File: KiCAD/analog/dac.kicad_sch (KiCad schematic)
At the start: 18 parts, among them Q11 2N3904, Q12 2N3904, U4 MCP4922-EP, U9 74HCT125

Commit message: revD analog: DGFET op-amp offset-mute topology + doc updates
Retire the Q11/Q12 PNP KeyUp mute path on the DGFET keyer G2 (sim showed
only ~2.6:1 on/off ratio with G1 biased above V_TO). Replace with an
LM7171 (U10) non-inverting op-amp wired as DC offset:
  V_G2 = V_DAC * (1 + R20/R23) - V_ref * (R20/R23)
with V_ref ~5.05V (1N4733A Zener D2, R24 1K bias, R25 1K / R32 100K
summing divider) and R20=6.2K / R23=10K (G=0.62). DAC=0 drives G2 to
-3.1V (fully cuts off the 40673, sim-verified 12pA leakage, ~10^9 on/off
ratio); DAC=5V drives G2 to +5V (matches prior keyed operating point).
KEY_UP net eliminated -- mute is intrinsic to the signal path, firmware
controls RF enable/disable solely via what it writes to the MCP4921
envelope channel.

Includes new test.kicad_sch sheet carrying the U10/R20-R32 subcircuit.

Doc updates: CLAUDE.md DGFET section rewritten; handoff doc gets a new
"DGFET keyer mute topology" section explaining retirement reason and
new transfer function; Master_Description Sec 2 and SPI-bus section
updated; revD_interconnect G2 amplitude-control block updated;
control_board_functional_blocks.md gets a prominent retirement banner
pointing at the current scheme.

Co-Authored-By: Claude Opus 4.7 <noreply@anthropic.com>
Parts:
- removed C51: 10uF, Capacitor_THT:CP_Radial_D5.0mm_P2.00mm, symbol Device:C_Polarized_US
- removed C92: 100nF, Capacitor_THT:C_Disc_D5.0mm_W2.5mm_P5.00mm, symbol Device:C_Small
- removed Q11, Q12: 2N3904, Package_TO_SOT_THT:TO-92_Inline_Wide, symbol Transistor_BJT:2N3904
- removed R48, R50, R51: 10K, Resistor_THT:R_Axial_DIN0207_L6.3mm_D2.5mm_P10.16mm_Horizontal, symbol Device:R_US
- removed R49: 47K, Resistor_THT:R_Axial_DIN0207_L6.3mm_D2.5mm_P10.16mm_Horizontal, symbol Device:R_US
- added C13, C14, C22: 10uF, symbol Device:C_Polarized
- added C15: 100nF, symbol Device:C
- added D3: 1N4733A, Diode_THT:D_DO-41_SOD81_P10.16mm_Horizontal, symbol xmitter:1N4728A
- added R22: 6.2K, symbol Device:R_US
- added R33, R34: 1K, symbol Device:R_US
- added R35: 100K, symbol Device:R_US
- added R36, R37: 10K, symbol Device:R_US
- added U11: LM7171xIN, Package_DIP:DIP-8_W7.62mm, symbol Amplifier_Operational:LM7171xIN
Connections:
- net +5V: now also C22.1
- net CS_DAC: now also R37.2
- net GND: now also C13.2, C14.1, C15.2, C22.2, D3.2 (A), R35.2
- net Gate 2: no longer names the net of R13.2
- net Gate 2: now also U11.3 (+); no longer TP20.1
- new net: R34.2, R35.1, R36.1
- new net: R22.1, R36.2, U11.2 (-)
- new net: C15.1, D3.1 (K), R33.2, R34.1
- new net +12V: C13.1, R33.1, U11.7 (V+)
- new net +3.3V: R37.1
- new net -12V: C14.2, U11.4 (V-)
- new net GATE_2: R22.2, TP20.1, U11.6

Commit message: revD: analog + ss_pa RF filtering on umbilical signals
ss_pa: 1 uH RFC + bypass cap(s) added on each umbilical-crossing signal
to attenuate 14 MHz ingress from the cable and keep hot IRF510-source
RF from being injected back into the umbilical:

- PA_Bias_A_Raw: L6 1uH + C13 100nF + C26 100pF at J31.7
- PA_Bias_B_Raw: L7 1uH + C22 100nF + C27 100pF at J31.8
- Source_Sense_A: L8 1uH + C23 100nF between IRF510A source tap and
  the shared comparator/ADC node (new Source_Sense_A_Raw holds the
  Kelvin sense resistors R1/R2)
- Source_Sense_B: L9 1uH + C24 100nF, mirror of A on Q4 side
- DRIVER_BIAS: R20 100R + C19 0.1uF + C20 100pF already placed
  previously
- FAULT_N: R23 100R + C25 100pF filter on the external side of the
  latch (LM393 outputs + R9 pullup remain on the internal node for
  fast latching, R23 isolates from umbilical and 4066 enables)

Attenuation ~40-60 dB at 14 MHz across all five umbilical signals.

Analog: companion schematic touches for the DGFET G2 op-amp mute
subcircuit on the test sheet.

Co-Authored-By: Claude Opus 4.7 <noreply@anthropic.com>
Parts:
- removed C13, C14: 10uF, symbol Device:C_Polarized
- added C13: 100pF, symbol Device:C
- added C24: 100nF, symbol Device:C
- added C25, C27: 0.1uF, symbol Device:C
- added R20: 100R, symbol Device:R_US
- U11: value LM7171xIN -> TL071CP
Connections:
- net +12V: now also C27.1
- net -12V: now also C25.2
- net GATE_2: now also C13.1, R20.2; no longer R22.2, TP20.1, U11.6
- net GND: now also C13.2, C24.2, C25.1, C27.2
- net at R34.2, R35.1, R36.1: now also C24.1
- new net: R20.1, R22.2, TP20.1, U11.6

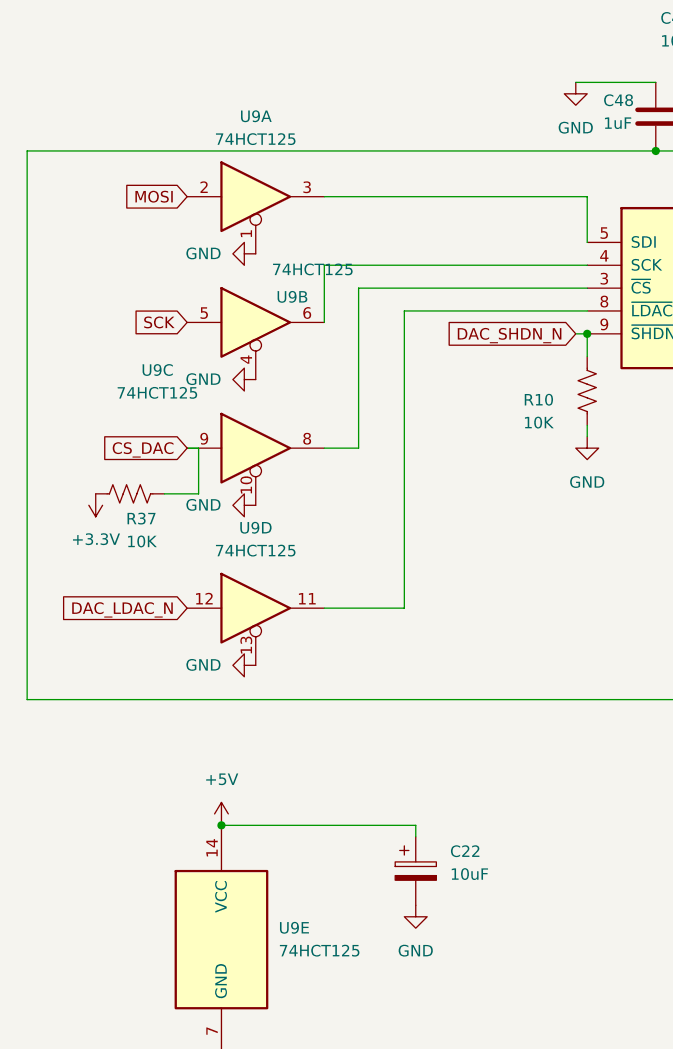
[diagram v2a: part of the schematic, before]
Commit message: revD analog: L1 Bourns 78F footprint + CD74HC4050E xmitter lib additions
Analog L1 (270nH Bourns 78F RF choke) gets footprint
Inductor_THT:L_Axial_L7.0mm_D3.3mm_P10.16mm_Horizontal_Fastron_MICC
(stock KiCad; 78F body 7.11x2.79mm fits within the MICC silk envelope).

Added to xmitter library:
- symbol CD74HC4050E (hex non-inverting buffer, DIP-16, standard 4050
  pinout, pre-linked to xmitter:DIP-16_W7.62mm footprint)
- footprint xmitter:DIP-16_W7.62mm (verbatim copy of stock
  Package_DIP:DIP-16_W7.62mm so the lib is self-contained)

Other sheet / project / netlist touches picked up from the recent
session work on analog test sheet and protoshield.

Co-Authored-By: Claude Opus 4.7 <noreply@anthropic.com>
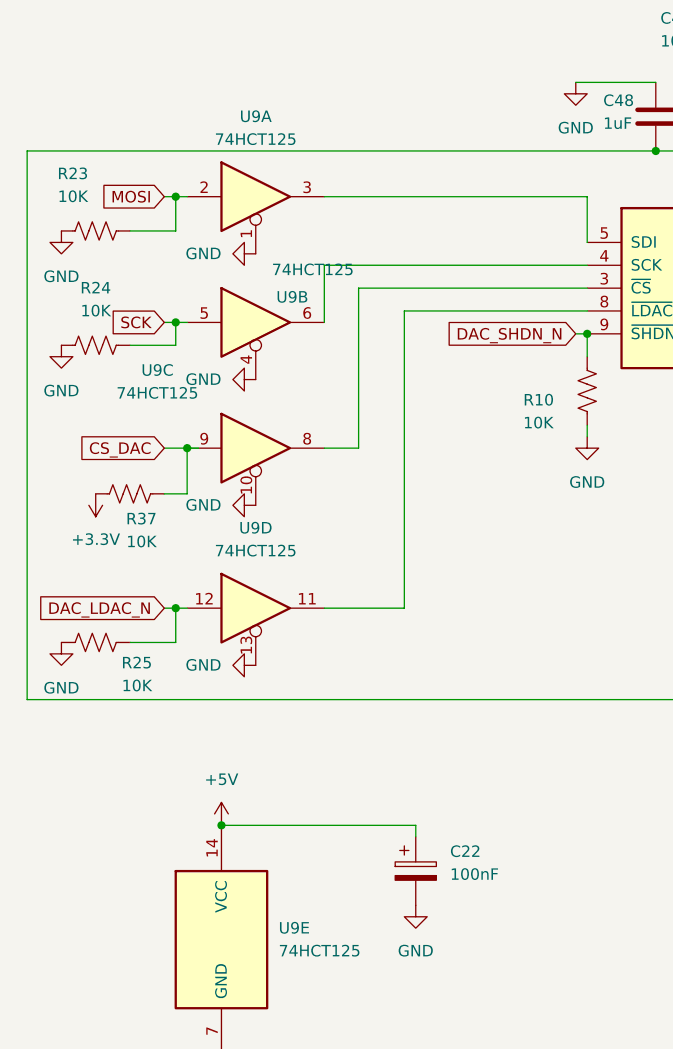
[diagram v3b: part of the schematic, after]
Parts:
- added R23, R24, R25: 10K, symbol Device:R_US
- C22: value 10uF -> 100nF
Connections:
- net DAC_LDAC_N: now also R25.2
- net GND: now also R23.1, R24.1, R25.1
- net MOSI: now also R23.2
- net SCK: now also R24.2

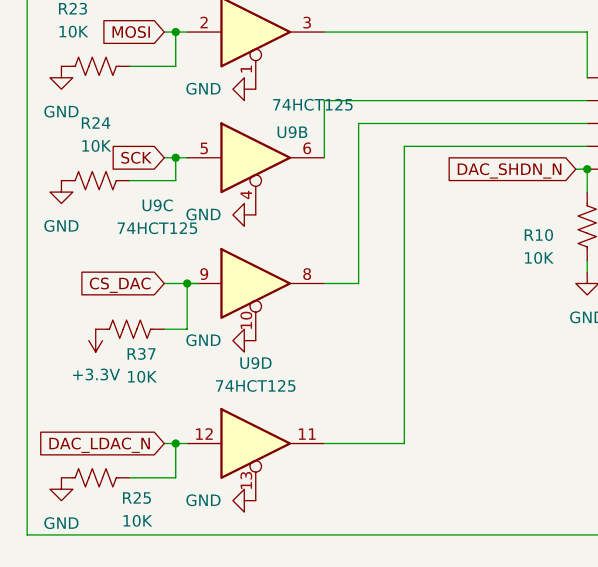
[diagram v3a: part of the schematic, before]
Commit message: revD: ss_pa U13 LM2936 pinout fix + analog U9 74HCT125 miswiring fix
ss_pa fault_shutdown.kicad_sch: fix U13 pin-to-signal mapping so an
LM2936Z-5.0/NOPB can be installed without destruction (prior MCP1700
symbol had pin 1=GND, 2=VI, 3=VO; LM2936 datasheet is pin 1=VO, 2=GND,
3=VI).

analog dac.kicad_sch: fix U9 74HCT125 miswiring found during follow-up
audit.

Co-Authored-By: Claude Opus 4.7 <noreply@anthropic.com>
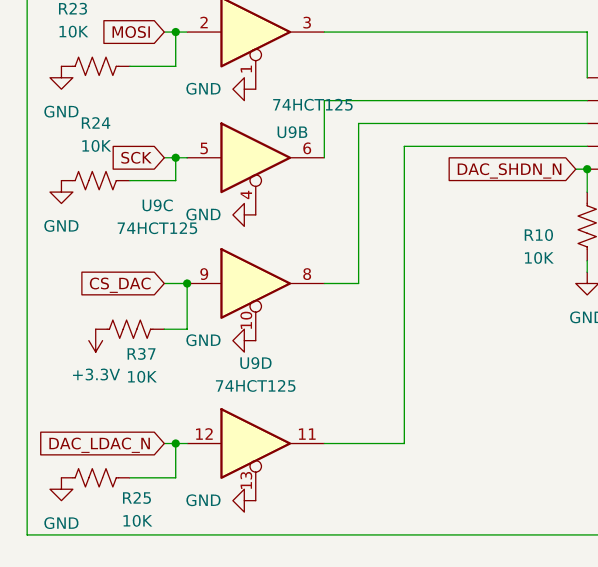
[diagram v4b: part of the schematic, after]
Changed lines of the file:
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@@
 	(wire
 		(pts
-			(xy 49.53 91.44) (xy 48.26 91.44)
-		)
-		(stroke
-			(width 0)
-			(type default)
-		)
-	)
-	(wire
-		(pts
 			(xy 46.99 63.5) (xy 48.26 63.5)
 		)
@@
 	)
 	(symbol
-		(lib_id "xmitter:74HCT125")
-		(at 55.88 91.44 0)
-		(unit 3)
-		(body_style 1)
-		(exclude_from_sim no)
-		(in_bom yes)
-		(on_board yes)
-		(in_pos_files yes)
-		(dnp no)
-		(property "Reference" "U9"
-			(at 44.958 82.804 0)
-			(show_name no)
-			(do_not_autoplace no)
-			(effects
-				(font
-					(size 1.27 1.27)
-				)
-			)
-		)
-		(property "Value" "74HCT125"
-			(at 44.958 85.344 0)
-			(show_name no)
-			(do_not_autoplace no)
-			(effects
-				(font
-					(size 1.27 1.27)
-				)
-			)
-		)
-		(property "Footprint" "xmitter:DIP-14_W7.62mm"
-			(at 55.88 91.44 0)
-			(hide yes)
-			(show_name no)
-			(do_not_autoplace no)
-			(effects
-				(font
-					(size 1.27 1.27)
-				)
-			)
-		)
-		(property "Datasheet" "https://www.ti.com/lit/ds/symlink/sn74hct125.pdf"
-			(at 55.88 91.44 0)
-			(hide yes)
-			(show_name no)
-			(do_not_autoplace no)
-			(effects
-				(font
-					(size 1.27 1.27)
-				)
-			)
-		)
-		(property "Description" "Quad bus buffer with 3-state outputs, TTL-level inputs (HCT family). Use for 3.3V to 5V unidirectional level shifting."
-			(at 55.88 91.44 0)
-			(hide yes)
-			(show_name no)
-			(do_not_autoplace no)
-			(effects
-				(font
-					(size 1.27 1.27)
-				)
-			)
-		)
-		(pin "3"
-		)
-		(pin "1"
-		)
-		(pin "2"
-		)
-		(pin "4"
-		)
-		(pin "9"
-		)
-		(pin "6"
-		)
-		(pin "14"
-		)
-		(pin "5"
-		)
-		(pin "12"
-		)
-		(pin "13"
-		)
-		(pin "8"
-		)
-		(pin "10"
-		)
-		(pin "7"
-		)
-		(pin "11"
-		)
-		(instances
-			(project "analog"
-				(path "/d3de40b8-856b-4fbd-829c-f45ffcd55742/e880f7dd-82a1-4efe-84f5-e6a9d5641736"
-					(reference "U9")
-					(unit 3)
-				)
-			)
-		)
-	)
-	(symbol
 		(lib_id "power:GND")
 		(at 128.27 107.95 0)
@@
 				)
 			)
+		)
+	)
+	(symbol
+		(lib_id "xmitter:74HCT125")
+		(at 55.88 91.44 0)
+		(unit 3)
+		(body_style 1)
+		(exclude_from_sim no)
+		(in_bom yes)
+		(on_board yes)
+		(in_pos_files yes)
+		(dnp no)
+		(property "Reference" "U9"
+			(at 44.958 82.804 0)
+			(show_name no)
+			(do_not_autoplace no)
+			(effects
+				(font
+					(size 1.27 1.27)
+				)
+			)
+		)
+		(property "Value" "74HCT125"
+			(at 44.958 85.344 0)
+			(show_name no)
+			(do_not_autoplace no)
+			(effects
+				(font
+					(size 1.27 1.27)
+				)
+			)
+		)
+		(property "Footprint" "xmitter:DIP-14_W7.62mm"
+			(at 55.88 91.44 0)
+			(hide yes)
+			(show_name no)
+			(do_not_autoplace no)
+			(effects
+				(font
+					(size 1.27 1.27)
+				)
+			)
+		)
+		(property "Datasheet" "https://www.ti.com/lit/ds/symlink/sn74hct125.pdf"
+			(at 55.88 91.44 0)
+			(hide yes)
+			(show_name no)
+			(do_not_autoplace no)
+			(effects
+				(font
+					(size 1.27 1.27)
+				)
+			)
+		)
+		(property "Description" "Quad bus buffer with 3-state outputs, TTL-level inputs (HCT family). Use for 3.3V to 5V unidirectional level shifting."
+			(at 55.88 91.44 0)
+			(hide yes)
+			(show_name no)
+			(do_not_autoplace no)
+			(effects
+				(font
+					(size 1.27 1.27)
+				)
+			)
+		)
+		(pin "3"
+		)
+		(pin "1"
+		)
+		(pin "2"
+		)
+		(pin "4"
+		)
+		(pin "9"
+		)
+		(pin "6"
+		)
+		(pin "14"
+		)
+		(pin "5"
+		)
+		(pin "12"
+		)
+		(pin "13"
+		)
+		(pin "8"
+		)
+		(pin "10"
+		)
+		(pin "7"
+		)
+		(pin "11"
+		)
+		(instances
+			(project "analog"
+				(path "/d3de40b8-856b-4fbd-829c-f45ffcd55742/e880f7dd-82a1-4efe-84f5-e6a9d5641736"
+					(reference "U9")
+					(unit 3)
+				)
+			)

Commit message: revD: footprint pass across all boards + ss_pa fault-chain fix + LLM review brief
- New tools/assign_misc_footprints.py: lib_id-keyed footprint assigner
  (resistors, screw terminals, pin headers, LT1054); mirrors cap-script
  safe-write (UTF-8 no BOM, no CRLF translation).
- tools/assign_cap_footprints.py: added 0.47uF -> C_Rect_L7.0mm case.
- Ran both scripts across analog, ss_pa, Output LPF, frontpanel,
  protoshield, and shelved power board. ~100 fills; details in diffs.
- ss_pa: R1-R4 (0.22 ohm source sense) upgraded to 2W Yageo RSF200
  with DIN0516 L15.5mm/P20.32mm footprint; Value tagged "0.22R 2W".
  R15/R16 confirmed 1/4W (DIN0207) for BS170 source degeneration.
- analog/power: R44 15R 5W horizontal, P30.48mm footprint.
- ss_pa fault chain (from external LLM review): R21/R22 raised
  10K -> 100K to restore self-latching loop gain; new R26 = 100K
  across C12 so cap discharges between power cycles (reliable reset).
  R26 footprint pending.
- Documentation/revD_llm_review_brief.md: new, comprehensive system
  description for external LLM deep-dive (function, component values,
  power dissipation, design flaws). References all five board netlists.

Co-Authored-By: Claude Opus 4.7 <noreply@anthropic.com>
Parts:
- C13: footprint (none) -> Capacitor_THT:C_Rect_L7.0mm_W3.5mm_P5.00mm
- C15, C22, C24, C25, C27: footprint (none) -> Capacitor_THT:C_Disc_D5.0mm_W2.5mm_P5.00mm
- R20, R22, R23, R24, R25, R33, R34, R35, R36, R37: footprint (none) -> Resistor_THT:R_Axial_DIN0207_L6.3mm_D2.5mm_P10.16mm_Horizontal
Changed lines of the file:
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@@
 			)
 		)
-		(property "Footprint" ""
+		(property "Footprint" "Resistor_THT:R_Axial_DIN0207_L6.3mm_D2.5mm_P10.16mm_Horizontal"
 			(at 146.304 99.314 90)
 			(hide yes)
@@
 			)
 		)
-		(property "Footprint" ""
+		(property "Footprint" "Resistor_THT:R_Axial_DIN0207_L6.3mm_D2.5mm_P10.16mm_Horizontal"
 			(at 38.354 78.994 90)
 			(hide yes)
@@
 			)
 		)
-		(property "Footprint" ""
+		(property "Footprint" "Resistor_THT:R_Axial_DIN0207_L6.3mm_D2.5mm_P10.16mm_Horizontal"
 			(at 38.354 66.294 90)
 			(hide yes)
@@
 			)
 		)
-		(property "Footprint" ""
+		(property "Footprint" "Resistor_THT:R_Axial_DIN0207_L6.3mm_D2.5mm_P10.16mm_Horizontal"
 			(at 38.354 112.014 90)
 			(hide yes)
@@
 			)
 		)
-		(property "Footprint" ""
+		(property "Footprint" "Capacitor_THT:C_Disc_D5.0mm_W2.5mm_P5.00mm"
 			(at 74.6252 142.24 0)
 			(hide yes)
@@
 			)
 		)
-		(property "Footprint" ""
+		(property "Footprint" "Resistor_THT:R_Axial_DIN0207_L6.3mm_D2.5mm_P10.16mm_Horizontal"
 			(at 129.286 96.774 90)
 			(hide yes)
@@
 			)
 		)
-		(property "Footprint" ""
+		(property "Footprint" "Resistor_THT:R_Axial_DIN0207_L6.3mm_D2.5mm_P10.16mm_Horizontal"
 			(at 157.734 118.364 90)
 			(hide yes)
@@
 			)
 		)
-		(property "Footprint" ""
+		(property "Footprint" "Resistor_THT:R_Axial_DIN0207_L6.3mm_D2.5mm_P10.16mm_Horizontal"
 			(at 174.244 96.774 90)
 			(hide yes)
@@
 			)
 		)
-		(property "Footprint" ""
+		(property "Footprint" "Capacitor_THT:C_Disc_D5.0mm_W2.5mm_P5.00mm"
 			(at 141.9352 107.95 0)
 			(hide yes)
@@
 			)
 		)
-		(property "Footprint" ""
+		(property "Footprint" "Resistor_THT:R_Axial_DIN0207_L6.3mm_D2.5mm_P10.16mm_Horizontal"
 			(at 42.164 95.504 90)
 			(hide yes)
@@
 			)
 		)
-		(property "Footprint" ""
+		(property "Footprint" "Capacitor_THT:C_Rect_L7.0mm_W3.5mm_P5.00mm"
 			(at 178.7652 105.41 0)
 			(hide yes)
@@
 			)
 		)
-		(property "Footprint" ""
+		(property "Footprint" "Capacitor_THT:C_Disc_D5.0mm_W2.5mm_P5.00mm"
 			(at 117.8052 107.95 0)
 			(hide yes)
@@
 			)
 		)
-		(property "Footprint" ""
+		(property "Footprint" "Capacitor_THT:C_Disc_D5.0mm_W2.5mm_P5.00mm"
 			(at 162.2552 86.36 0)
 			(hide yes)
@@
 			)
 		)
-		(property "Footprint" ""
+		(property "Footprint" "Resistor_THT:R_Axial_DIN0207_L6.3mm_D2.5mm_P10.16mm_Horizontal"
 			(at 136.906 104.394 90)
 			(hide yes)
@@
 			)
 		)
-		(property "Footprint" ""
+		(property "Footprint" "Capacitor_THT:C_Disc_D5.0mm_W2.5mm_P5.00mm"
 			(at 187.6552 86.36 0)
 			(hide yes)
@@
 			)
 		)
-		(property "Footprint" ""
+		(property "Footprint" "Resistor_THT:R_Axial_DIN0207_L6.3mm_D2.5mm_P10.16mm_Horizontal"
 			(at 132.334 99.314 90)
 			(hide yes)
